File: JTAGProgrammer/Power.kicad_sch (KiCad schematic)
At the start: 22 parts, among them U2 LP2985-3.3, U8 LP2985-2.5

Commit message: Add LCSC part numbers
Signed-off-by: Anthony Bernaert <anthony.bernaert@gmail.com>
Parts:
- FB1: LCSC (none) -> C107335
- U2: LCSC (none) -> C95414
- U8: LCSC (none) -> C2863838
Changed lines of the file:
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@@
+      (effects (font (size 1.27 1.27)) hide)
+    )
+    (property "LCSC" "C2863838" (at 131.445 120.65 0)
       (effects (font (size 1.27 1.27)) hide)
     )
@@
       (effects (font (size 1.27 1.27)) hide)
     )
+    (property "LCSC" "C107335" (at 80.645 88.265 90)
+      (effects (font (size 1.27 1.27)) hide)
+    )
     (pin "1")
     (pin "2")
@@
     )
     (property "Datasheet" "http://www.ti.com/lit/ds/symlink/lp2985.pdf" (at 131.445 90.805 0)
+      (effects (font (size 1.27 1.27)) hide)
+    )
+    (property "LCSC" "C95414" (at 131.445 90.805 0)
       (effects (font (size 1.27 1.27)) hide)
     )
@@
       (effects (font (size 1.27 1.27)) hide)
     )
+    (property "LCSC" "C107335" (at 183.515 71.755 90)
+      (effects (font (size 1.27 1.27)) hide)
+    )
     (pin "1")
     (pin "2")
@@
       (effects (font (size 1.27 1.27)) hide)
     )
+    (property "LCSC" "C107335" (at 182.245 88.265 90)
+      (effects (font (size 1.27 1.27)) hide)
+    )

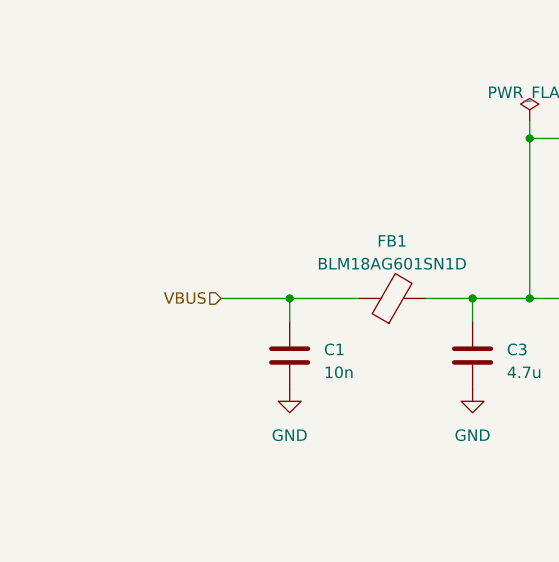
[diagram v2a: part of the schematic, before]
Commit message: Rev.2: change to USB Type-C, add VBUS fuse, VREF LED indicators
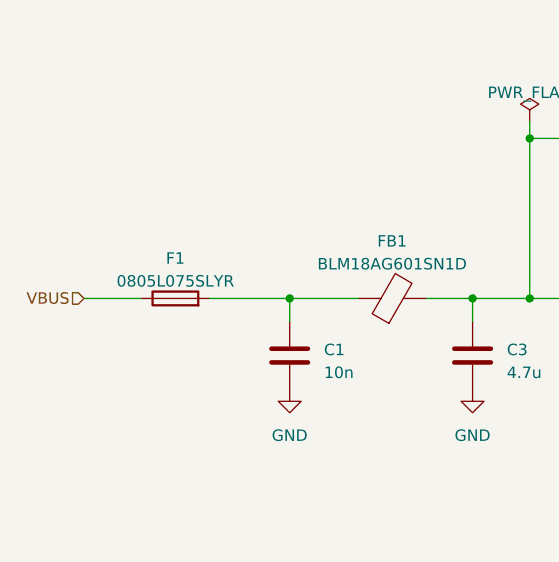
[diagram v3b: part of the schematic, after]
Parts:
- added F1: 0805L075SLYR, Fuse:Fuse_0805_2012Metric, symbol Device:Fuse
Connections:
- net VBUS: now also F1.1; no longer C1.1, FB1.1
- new net: C1.1, F1.2, FB1.1
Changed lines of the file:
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@@
     (title "FTDI JTAG Programmer")
     (date "2024-10-11")
-    (rev "1.1")
+    (rev "2")
   )
   (junction (at 228.6 71.755) (diameter 0) (color 0 0 0 0)
   )
+  (junction (at 194.945 88.265) (diameter 0) (color 0 0 0 0)
+  )
+  (junction (at 197.485 71.755) (diameter 0) (color 0 0 0 0)
+  )
+  (junction (at 167.005 118.11) (diameter 0) (color 0 0 0 0)
+  )
+  (junction (at 113.03 118.11) (diameter 0) (color 0 0 0 0)
+  )
+  (junction (at 109.855 88.265) (diameter 0) (color 0 0 0 0)
+  )
+  (junction (at 95.885 88.265) (diameter 0) (color 0 0 0 0)
+  )
+  (junction (at 219.075 71.755) (diameter 0) (color 0 0 0 0)
+  )
   (junction (at 69.215 88.265) (diameter 0) (color 0 0 0 0)
   )
-  (junction (at 194.945 88.265) (diameter 0) (color 0 0 0 0)
-  )
-  (junction (at 197.485 71.755) (diameter 0) (color 0 0 0 0)
-  )
-  (junction (at 167.005 118.11) (diameter 0) (color 0 0 0 0)
-  )
-  (junction (at 113.03 118.11) (diameter 0) (color 0 0 0 0)
-  )
-  (junction (at 109.855 88.265) (diameter 0) (color 0 0 0 0)
-  )
-  (junction (at 95.885 88.265) (diameter 0) (color 0 0 0 0)
-  )
-  (junction (at 219.075 71.755) (diameter 0) (color 0 0 0 0)
-  )
   (junction (at 205.74 71.755) (diameter 0) (color 0 0 0 0)
   )
@@
   (junction (at 228.6 88.265) (diameter 0) (color 0 0 0 0)
   )
+  (wire (pts (xy 46.355 88.265) (xy 52.705 88.265))
+    (stroke (width 0) (type default))
+  )
   (wire (pts (xy 141.605 120.65) (xy 144.145 120.65))
     (stroke (width 0) (type default))
@@
     (stroke (width 0) (type default))
   )
-  (wire (pts (xy 61.595 88.265) (xy 69.215 88.265))
-    (stroke (width 0) (type default))
-  )
   (wire (pts (xy 205.74 71.755) (xy 212.725 71.755))
     (stroke (width 0) (type default))
@@
   )
   (wire (pts (xy 69.215 88.265) (xy 76.835 88.265))
+    (stroke (width 0) (type default))
+  )
+  (wire (pts (xy 60.325 88.265) (xy 69.215 88.265))
     (stroke (width 0) (type default))
   )
@@
     (effects (font (size 1.27 1.27)) (justify left))
   )
-  (hierarchical_label "VBUS" (shape input) (at 61.595 88.265 180) (fields_autoplaced)
+  (hierarchical_label "VBUS" (shape input) (at 46.355 88.265 180) (fields_autoplaced)
     (effects (font (size 1.27 1.27)) (justify right))
   )
@@
     )
   )
+  (netclass_flag "" (length 2.54) (shape round) (at 69.215 88.265 0)
+    (effects (font (size 1.27 1.27)) (justify left bottom))
+    (property "Netclass" "POWER" (at 64.77 83.82 0)
+      (effects (font (size 1.27 1.27) italic) (justify left))
+    )
+  )
   (netclass_flag "" (length 2.54) (shape round) (at 155.575 118.11 0) (fields_autoplaced)
     (effects (font (size 1.27 1.27)) (justify left bottom))
@@
         )
       )
+    )
+  )
+  (symbol (lib_id "Device:Fuse") (at 56.515 88.265 90) (unit 1)
+    (in_bom yes) (on_board yes) (dnp no) (fields_autoplaced)
+    (property "Reference" "F1" (at 56.515 83.82 90)
+      (effects (font (size 1.27 1.27)))
+    )
+    (property "Value" "0805L075SLYR" (at 56.515 86.36 90)
+      (effects (font (size 1.27 1.27)))
+    )
+    (property "Footprint" "Fuse:Fuse_0805_2012Metric" (at 56.515 90.043 90)
+      (effects (font (size 1.27 1.27)) hide)
+    )
+    (property "Datasheet" "~" (at 56.515 88.265 0)
+      (effects (font (size 1.27 1.27)) hide)
+    )
+    (property "LCSC" "C2843994" (at 56.515 88.265 90)
+      (effects (font (size 1.27 1.27)) hide)
+    )
+    (pin "1")
+    (pin "2")
+    (instances
+      (project "JTAGProgrammer"
+        (path "/57e59b41-6264-486e-a79b-29cd6022f5d7/f95d4af7-719b-4407-a433-56afc9794200"
+          (reference "F1") (unit 1)
+        )
+      )
